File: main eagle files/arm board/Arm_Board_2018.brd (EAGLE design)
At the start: 193.8 x 103.9 mm, 151 parts, among them Q1 Q_IRF7437SMD, U1 TIVA-1294, U4 ACS722, U5 ACS722, U6 ACS722, U7 ACS722, U8 ACS722, U9 ACS722

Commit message: Further progress
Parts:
- removed OE_PULLUP: 10K, SparkFun-Passives:0402-RES
- moved C5 19.6 mm to (136.1, 5.08), turned to 90 degrees
- moved C6 15.8 mm to (136.1, 12.7), turned to 270 degrees
- moved R69 13.9 mm to (158.0, 6.86), turned to 180 degrees
- moved R70 12.9 mm to (158.0, 14.5), turned to 180 degrees
- moved R54 12.6 mm to (31.5, 86.9), turned to 90 degrees
- moved R50 10.4 mm to (158.0, 9.91), turned to 0 degrees
- moved S5 9.67 mm to (13.5, 88.9), turned to 270 degrees
- moved R60 9.00 mm to (158.0, 13.0), turned to 180 degrees
- moved R33 8.39 mm to (105.9, 73.2), turned to 180 degrees
- moved R29 8.36 mm to (105.9, 76.2), turned to 0 degrees
- moved R34 7.50 mm to (105.9, 80.8), turned to 180 degrees
- moved R32 7.37 mm to (105.9, 77.7), turned to 180 degrees
- moved R67 6.84 mm to (158.0, 8.38), turned to 180 degrees
- moved S4 6.71 mm to (33.3, 89.7), turned to 270 degrees
- moved R55 6.14 mm to (24.4, 86.9), turned to 90 degrees
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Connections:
- removed net MOTOR7_POWER: C6.1, MOT7_HB.12, MOT7_HB.13, MOT7_HB.23, MOT7_HB.3, MOT7_HB.VCC, MOT7_HB.VCC@1
- removed net MOTOR8_POWER: C5.1, MOT8_HB.12, MOT8_HB.13, MOT8_HB.23, MOT8_HB.3, MOT8_HB.VCC, MOT8_HB.VCC@1
- removed net PWM_OUTPUT_ENABLE: OE_PULLUP.2, PWM_DRIVER.23
- net 12VMOTOR_POWER: now also C5.1, C6.1, MOT7_HB.12, MOT7_HB.13, MOT7_HB.23, MOT7_HB.3, MOT7_HB.VCC, MOT7_HB.VCC@1, MOT8_HB.12, MOT8_HB.13, MOT8_HB.23, MOT8_HB.3, MOT8_HB.VCC, MOT8_HB.VCC@1
- net BUTTON1: now also U1.PM2
- net BUTTON2: now also U1.PM1
- net BUTTON3: now also U1.PM0
- net ENCODER_1: now also U1.PL4
- net ENCODER_2: now also U1.PD2
- net ENCODER_3: now also U1.PA4
- net ENCODER_4: now also U1.PA6
- net ENCODER_5: now also U1.PM4
- net ENCODER_6: now also U1.PB2
- net GND: now also PWM_DRIVER.23, U1.GND_1, U1.GND_2, U1.GND_3, U1.GND_4
- net LED1: now also U1.PB4
- net LED2: now also U1.PB5
- net LED3: now also U1.PD4
- net LED4: now also U1.PD5
- net LED5: now also U1.PQ0
- net LED6: now also U1.PP4
- net LIMIT_SWITCH_1: now also U1.PB3
- net LIMIT_SWITCH_2: now also U1.PC7
- net LIMIT_SWITCH_3: now also U1.PD3
- net LOGIC_3.3V: now also U1.+3V3_1, U1.+3V3_2; no longer OE_PULLUP.1
- net MAINLINE_CURRENT_SENSOR: now also U1.PK3
- net MASTER_POWER_ENABLE: now also U1.PQ1
- net MOTOR1_CURRENT_SENSOR: now also U1.PK2
- net MOTOR1_INA: now also U1.PQ2/PA3
- net MOTOR1_INB: now also U1.PQ3/PA2
- net MOTOR2_CURRENT_SENSOR: now also U1.PK1
- net MOTOR2_INA: now also U1.PK4
- net MOTOR2_INB: now also U1.PK5
- net MOTOR3_CURRENT_SENSOR: now also U1.PK0
- net MOTOR3_INA: now also U1.PC4
- net MOTOR3_INB: now also U1.PC5
- net MOTOR4_CURRENT_SENSOR: now also U1.PE2
- net MOTOR4_INA: now also U1.PC6
- net MOTOR4_INB: now also U1.PE5
- net MOTOR5_CURRENT_SENSOR: now also U1.PE1
- net MOTOR5_INA: now also U1.PE3
- net MOTOR5_INB: now also U1.PM5
- net MOTOR6_CURRENT_SENSOR: now also U1.PE0
- net MOTOR6_INA: now also U1.PF1
- net MOTOR6_INB: now also U1.PF2
- net MOTOR7_INA: now also U1.PH2
- net MOTOR7_INB: now also U1.PH3
- net MOTOR8_INA: now also U1.PD1
- net MOTOR8_INB: now also U1.PD0
- net PWM_DRIVER_SCL: now also U1.PN5
- net PWM_DRIVER_SDA: now also U1.PN4
- net SWITCH: now also U1.PH0
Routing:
- net LOGIC_3.3V: track 336.5 -> 765.9 mm, vias 8 -> 15
- net 12VMOTOR_POWER: track 0.00 -> 167.1 mm, vias 53 -> 68
- net MOTOR1_CURRENT_SENSOR: track 5.25 -> 107.0 mm, vias 0 -> 3
- net MAINLINE_CURRENT_SENSOR: track 0.00 -> 99.0 mm, vias 0 -> 3
- net MOTOR3_CURRENT_SENSOR: track 6.40 -> 101.4 mm
- net MOTOR2_CURRENT_SENSOR: track 7.78 -> 98.6 mm
- net MOTOR8_INB: track 0.00 -> 85.4 mm, vias 0 -> 2
- net MOTOR8_INA: track 0.00 -> 81.7 mm, vias 0 -> 2
- net MOTOR4_CURRENT_SENSOR: track 0.00 -> 76.4 mm, vias 0 -> 1
- net MOTOR3_INB: track 0.00 -> 74.1 mm, vias 0 -> 1
- net ENCODER_1: track 0.00 -> 69.5 mm, vias 0 -> 2
- net MOTOR3_INA: track 0.00 -> 65.3 mm, vias 0 -> 1
- net MOTOR5_CURRENT_SENSOR: track 5.78 -> 67.9 mm, vias 0 -> 1
- net MOTOR6_CURRENT_SENSOR: track 17.5 -> 75.7 mm
- net MOTOR7_2: track 0.00 -> 58.1 mm, vias 0 -> 1
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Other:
- board size 193.8 x 103.9 mm -> 193.8 x 104.4 mm

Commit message: all things routed
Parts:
- added H1: MOUNTING_HOLE#6, MRDT-Hardware:#6_SCREW
- added LOGO1: MRDT_LOGO, MRDT-Hardware:MRDT_LOGO
- moved SCL_PULLUP 18.2 mm to (76.2, 81.3), turned to 90 degrees
- moved PWM_DRIVER 16.3 mm to (85.1, 78.2)
- moved SDA_PULLUP 4.49 mm to (73.7, 81.3), turned to 90 degrees
- moved R6 0.51 mm to (60.2, 40.9)
- moved C6 0.51 mm to (136.1, 12.2)
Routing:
- net MOTOR3_POWER: track 196.4 -> 374.3 mm, vias 7 -> 17
- net MOTOR4_POWER: track 161.3 -> 296.1 mm, vias 6 -> 14
- net MOTOR8_PWM: track 0.00 -> 124.3 mm, vias 0 -> 2
- net MOTOR3_PWM: track 0.00 -> 120.4 mm, vias 0 -> 2
- net MOTOR7_PWM: track 0.00 -> 96.3 mm, vias 0 -> 2
- net MOTOR4_PWM: track 0.00 -> 92.2 mm, vias 0 -> 2
- net MOTOR2_2: track 94.0 -> 182.7 mm, vias 0 -> 3
- net MOTOR5_2: track 88.7 -> 170.1 mm, vias 3 -> 6
- net MOTOR5_POWER: track 103.7 -> 180.4 mm, vias 6 -> 12
- net 12VMOTOR_POWER: track 167.1 -> 242.6 mm, vias 68 -> 72
- net PWM_DRIVER_SDA: track 0.00 -> 63.8 mm, vias 0 -> 2
- net MOTOR5_1: track 66.5 -> 127.5 mm, vias 0 -> 3
- net PWM_DRIVER_SCL: track 0.00 -> 59.7 mm, vias 0 -> 2
- net MOTOR4_2: track 73.1 -> 130.0 mm, vias 0 -> 3
- net MOTOR6_PWM: track 9.21 -> 63.6 mm, vias 0 -> 3
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
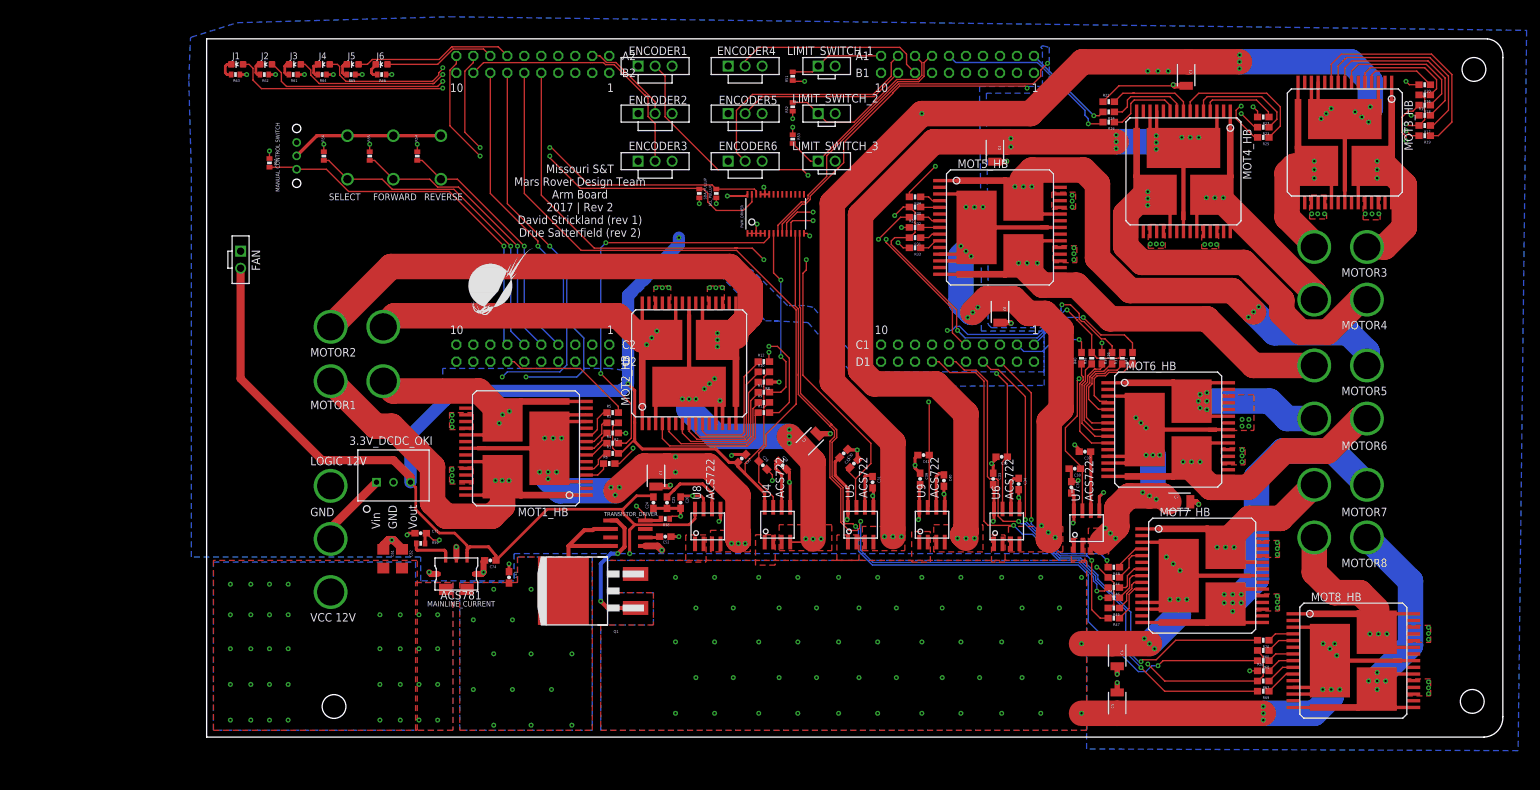
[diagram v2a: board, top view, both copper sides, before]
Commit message: reworked on board text, added space for ethernet
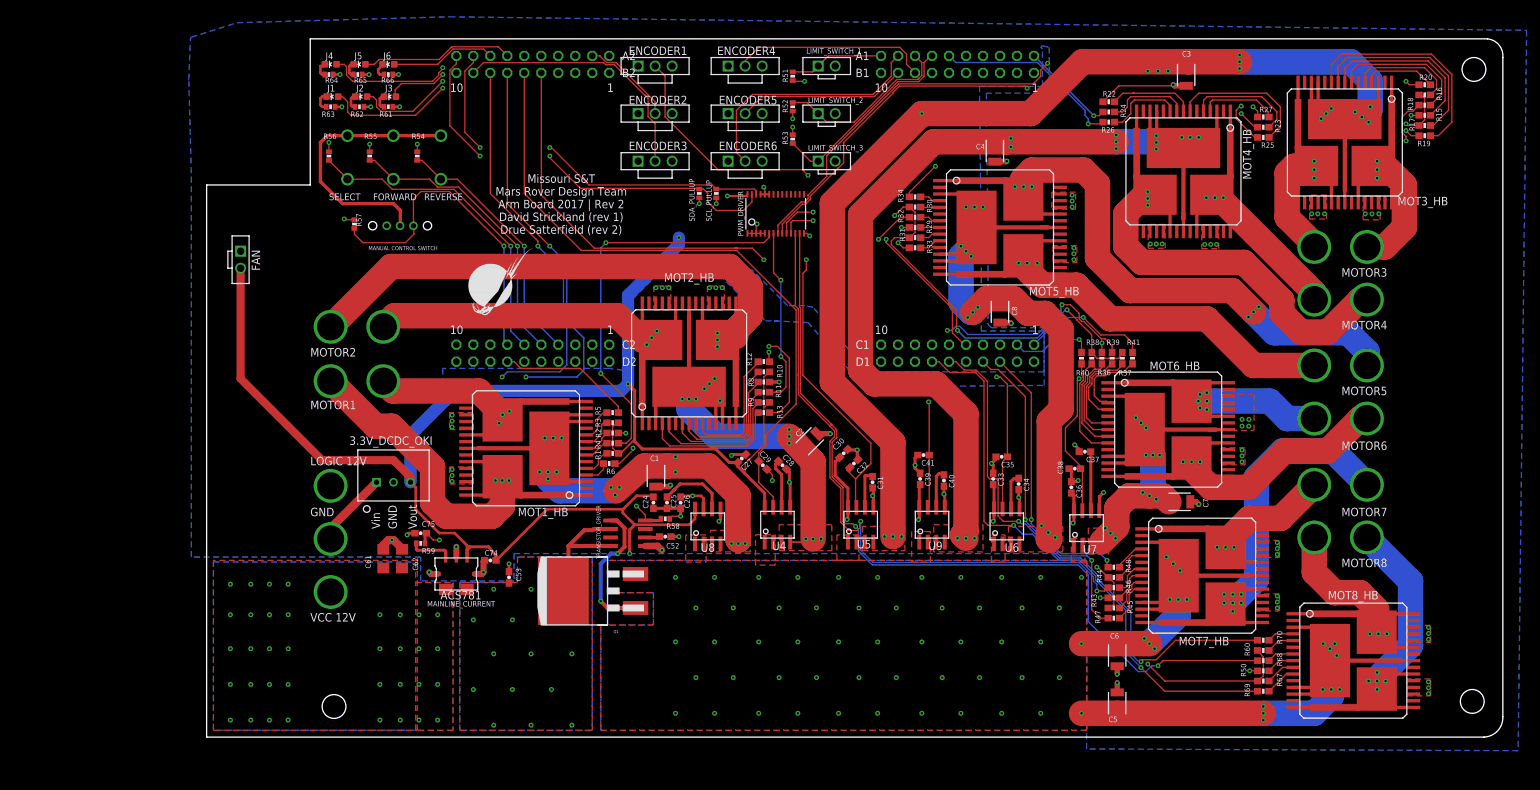
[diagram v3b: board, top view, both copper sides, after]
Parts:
- moved S5 18.3 mm to (26.9, 76.5), turned to 0 degrees
- moved R57 15.6 mm to (22.1, 76.7)
- moved R63 15.0 mm to (18.5, 94.2)
- moved D1 15.0 mm to (18.8, 95.8)
- moved D2 15.0 mm to (23.1, 95.8)
- moved R61 15.0 mm to (27.2, 94.2)
- moved R62 15.0 mm to (22.9, 94.2)
- moved D3 15.0 mm to (27.4, 95.8)
- moved D4 1.02 mm to (18.5, 100.6)
- moved D6 1.02 mm to (27.2, 100.6)
- moved R64 1.02 mm to (18.3, 99.1)
- moved R65 1.02 mm to (22.6, 99.1)
- moved R66 1.02 mm to (27.2, 99.1)
- moved D5 1.02 mm to (22.9, 100.6)
- moved R56 0.76 mm to (18.3, 86.9)
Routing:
- net LOGIC_3.3V: track 771.7 -> 789.2 mm
- net LED3: track 39.4 -> 25.0 mm
- net LED2: track 45.8 -> 32.6 mm
- net LED1: track 53.2 -> 40.1 mm
- net SWITCH: track 54.9 -> 48.7 mm
- net LED4: track 32.8 -> 31.8 mm
- net LED5: track 23.9 -> 22.9 mm
- net LED6: track 16.7 -> 15.7 mm
- net BUTTON1: track 48.8 -> 48.1 mm
- net GND: track 118.1 -> 118.8 mm
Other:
- outline, holes or cut-outs redrawn

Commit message: added more polygons
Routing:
- net MOTOR4_POWER: track 296.1 -> 308.0 mm, vias 14 -> 18
- net MOTOR3_POWER: track 374.3 -> 385.0 mm, vias 17 -> 20
- net MOTOR6_POWER: track 96.2 -> 89.4 mm, vias 12 -> 15
- net MOTOR2_POWER: track 135.4 -> 139.5 mm, vias 13 -> 14
- net MOTOR5_POWER: track 180.4 -> 177.2 mm, vias 12 -> 17
- net MOTOR1_POWER: track 146.1 -> 148.6 mm, vias 15 -> 18
- net 12VMOTOR_POWER: track 242.6 -> 244.8 mm, vias 72 -> 79
- net MOTOR2_2: track 182.7 -> 183.2 mm
- added copper zone on layer 2, net MOTOR1_POWER
- added copper zone on layer 2, net MOTOR2_POWER
- added copper zone on layer 2, net MOTOR3_POWER
- added copper zone on layer 2, net MOTOR4_POWER
- added copper zone on layer 2, net MOTOR5_POWER
- added copper zone on layer 2, net MOTOR6_POWER

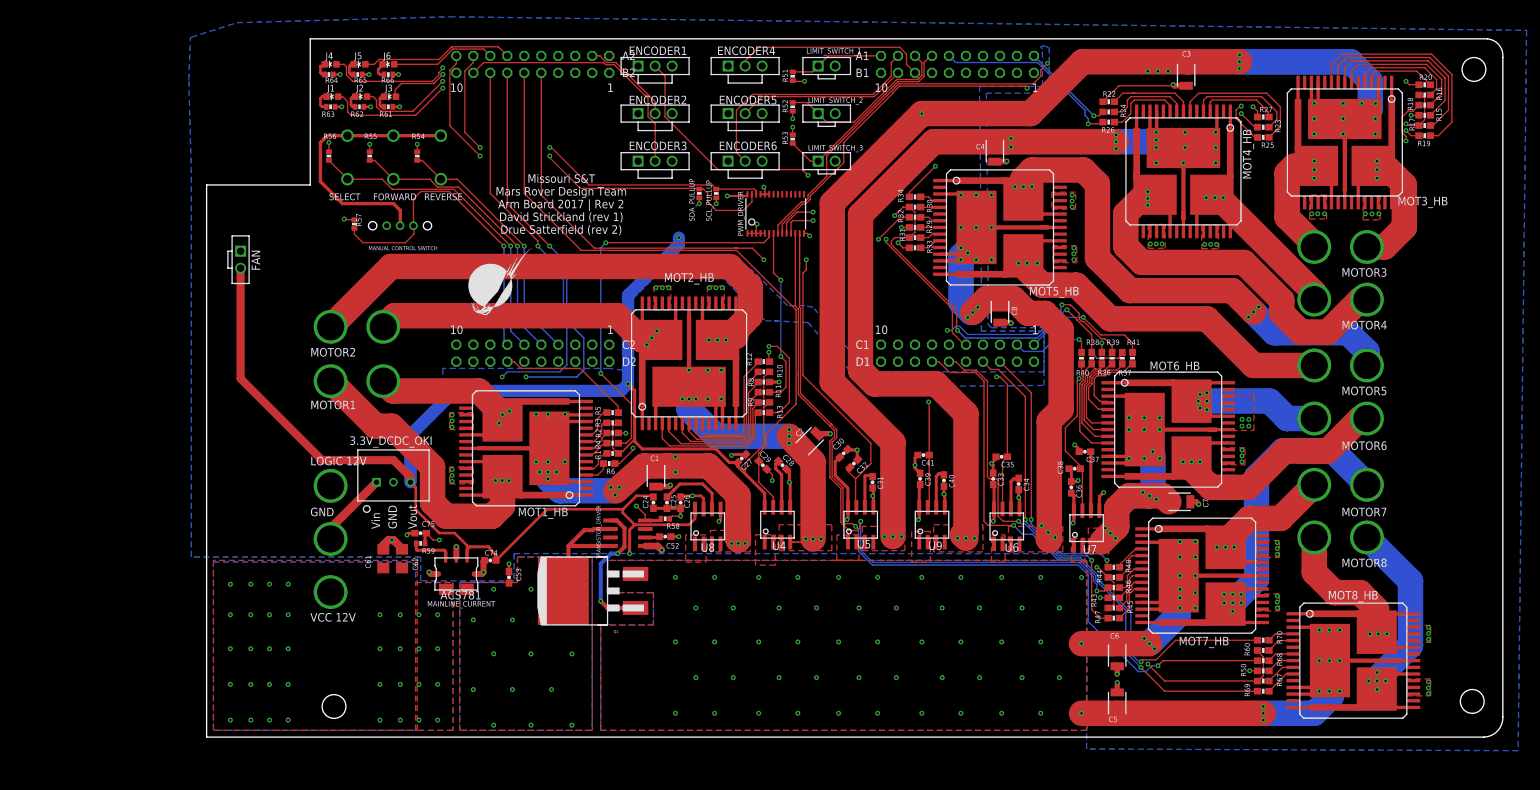
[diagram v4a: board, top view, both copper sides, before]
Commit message: Revert "added more polygons"
This reverts commit 0127a168e7661bc7332a66d9e3b5fca905d482c1.
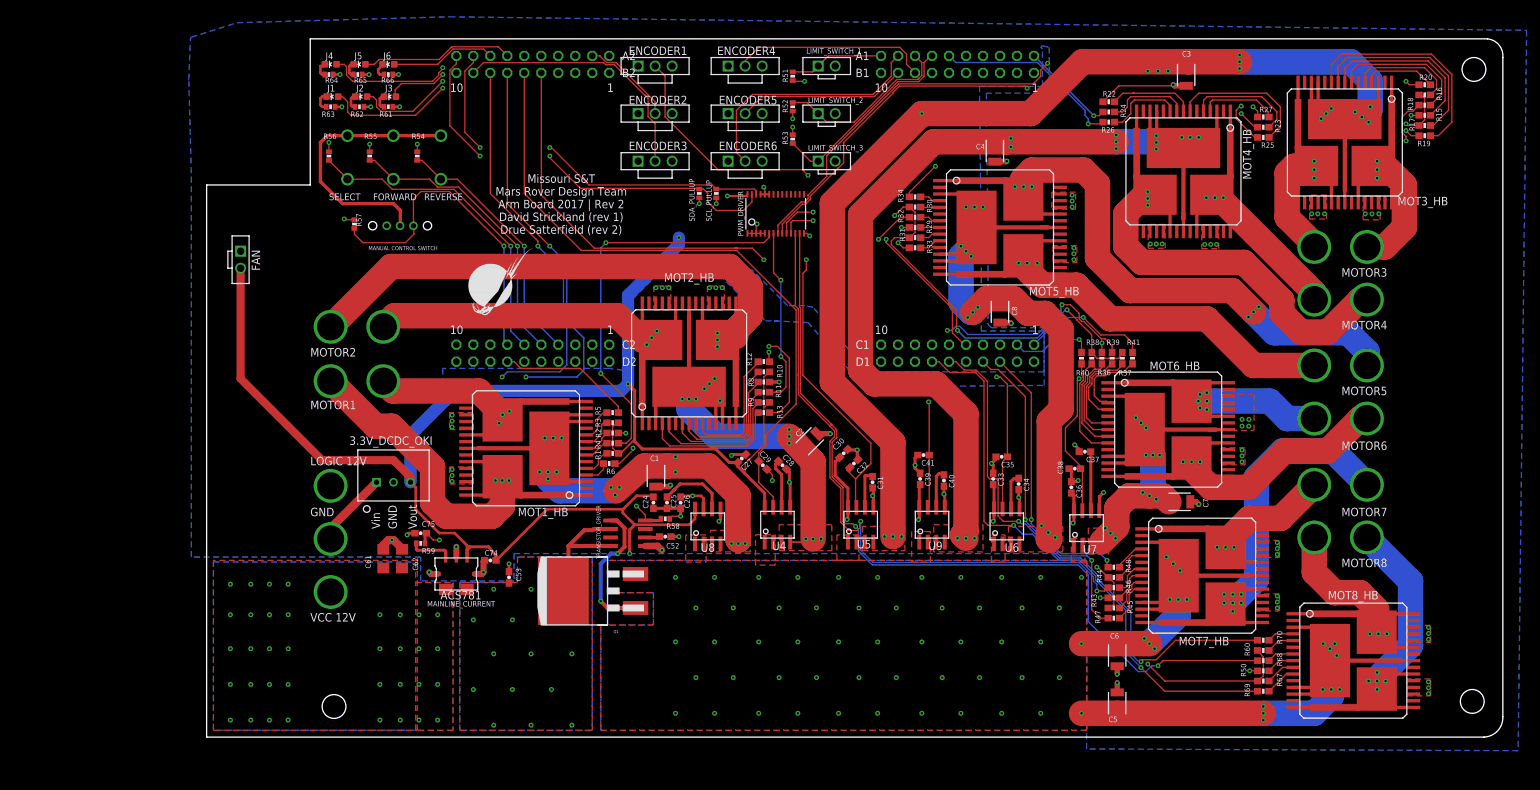
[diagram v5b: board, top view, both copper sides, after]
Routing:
- net MOTOR4_POWER: track 308.0 -> 296.1 mm, vias 18 -> 14
- net MOTOR3_POWER: track 385.0 -> 374.3 mm, vias 20 -> 17
- net MOTOR6_POWER: track 89.4 -> 96.2 mm, vias 15 -> 12
- net MOTOR2_POWER: track 139.5 -> 135.4 mm, vias 14 -> 13
- net MOTOR5_POWER: track 177.2 -> 180.4 mm, vias 17 -> 12
- net MOTOR1_POWER: track 148.6 -> 146.1 mm, vias 18 -> 15
- net 12VMOTOR_POWER: track 244.8 -> 242.6 mm, vias 79 -> 72
- net MOTOR2_2: track 183.2 -> 182.7 mm
- removed copper zone on layer 2, net MOTOR1_POWER
- removed copper zone on layer 2, net MOTOR2_POWER
- removed copper zone on layer 2, net MOTOR3_POWER
- removed copper zone on layer 2, net MOTOR4_POWER
- removed copper zone on layer 2, net MOTOR5_POWER
- removed copper zone on layer 2, net MOTOR6_POWER
